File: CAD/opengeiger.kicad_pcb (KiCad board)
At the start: 2 copper layers, 91 x 43 mm, 58 parts, among them J1 Conn_01x02, J10 Conn_01x04, J2 Conn_01x02, J3 Conn_01x06, J4 Conn_01x02, J5 Conn_01x04, J6 Conn_01x04, J7 Conn_01x02, J8 USB_C_Receptacle_USB2.0, J9 Conn_01x04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

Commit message: feat: added interactive html bom
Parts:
- added R18: 10k, Resistor_SMD:R_0603_1608Metric_Pad0.98x0.95mm_HandSolder, F.Cu at (134.1, 102.4)
- Q3: value PMBT2222A,215 -> SI2301
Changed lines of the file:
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@@
     (tags "SOT-23")
     (property "INFO" "DIGIKEY")
-    (property "MPN" "PMBT2222A,215")
-    (property "Sheetfile" "opengeiger.kicad_sch")
-    (property "Sheetname" "")
-    (property "Supplier Part Number" "1727-2956-6-ND")
+    (property "MPN" "SI2302CDS-T1-GE3")
+    (property "Sheetfile" "opengeiger.kicad_sch")
+    (property "Sheetname" "")
+    (property "Supplier Part Number" "SI2302CDS-T1-GE3DKR-ND")
     (attr smd)
     (fp_text reference "Q3" (at 3.602 -1.362) (layer "F.SilkS")
       (effects (font (size 1 1) (thickness 0.15)))
     )
-    (fp_text value "PMBT2222A,215" (at 0 2.5) (layer "F.Fab")
+    (fp_text value "SI2301" (at 0 2.5) (layer "F.Fab")
       (effects (font (size 1 1) (thickness 0.15)))
     )
@@
       (net 16 "Net-(D5-Pad2)") (pintype "passive"))
     (model "${KIPRJMOD}/packages3D/R_0603_1608Metric.wrl"
+      (offset (xyz 0 0 0))
+      (scale (xyz 1 1 1))
+      (rotate (xyz 0 0 0))
+    )
+  )
+  (footprint "Resistor_SMD:R_0603_1608Metric_Pad0.98x0.95mm_HandSolder" (layer "F.Cu")
+    (at 134.112 102.362 90)
+    (descr "Resistor SMD 0603 (1608 Metric), square (rectangular) end terminal, IPC_7351 nominal with elongated pad for handsoldering. (Body size source: IPC-SM-782 page 72, https://www.pcb-3d.com/wordpress/wp-content/uploads/ipc-sm-782a_amendment_1_and_2.pdf), generated with kicad-footprint-generator")
+    (tags "resistor handsolder")
+    (property "INFO" "DIGIKEY")
+    (property "MPN" "RMCF0603JT10K0")
+    (property "Sheetfile" "opengeiger.kicad_sch")
+    (property "Sheetname" "")
+    (property "Supplier Part Number" "RMCF0603JT10K0DKR-ND")
+    (attr smd)
+    (fp_text reference "R18" (at 0 -1.43 90) (layer "F.SilkS")
+      (effects (font (size 1 1) (thickness 0.15)))
+    )
+    (fp_text value "10k" (at 0 1.43 90) (layer "F.Fab")
+      (effects (font (size 1 1) (thickness 0.15)))
+    )
+    (fp_text user "${REFERENCE}" (at 0 0 90) (layer "F.Fab")
+      (effects (font (size 0.4 0.4) (thickness 0.06)))
+    )
+    (fp_line (start -0.254724 -0.5225) (end 0.254724 -0.5225) (layer "F.SilkS") (width 0.12))
+    (fp_line (start -0.254724 0.5225) (end 0.254724 0.5225) (layer "F.SilkS") (width 0.12))
+    (fp_line (start 1.65 0.73) (end -1.65 0.73) (layer "F.CrtYd") (width 0.05))
+    (fp_line (start 1.65 -0.73) (end 1.65 0.73) (layer "F.CrtYd") (width 0.05))
+    (fp_line (start -1.65 0.73) (end -1.65 -0.73) (layer "F.CrtYd") (width 0.05))
+    (fp_line (start -1.65 -0.73) (end 1.65 -0.73) (layer "F.CrtYd") (width 0.05))
+    (fp_line (start 0.8 0.4125) (end -0.8 0.4125) (layer "F.Fab") (width 0.1))
+    (fp_line (start -0.8 0.4125) (end -0.8 -0.4125) (layer "F.Fab") (width 0.1))
+    (fp_line (start -0.8 -0.4125) (end 0.8 -0.4125) (layer "F.Fab") (width 0.1))
+    (fp_line (start 0.8 -0.4125) (end 0.8 0.4125) (layer "F.Fab") (width 0.1))
+    (pad "1" smd roundrect (at -0.9125 0 90) (size 0.975 0.95) (layers "F.Cu" "F.Paste" "F.Mask") (roundrect_rratio 0.25)
+      (net 2 "GNDREF") (pintype "passive"))
+    (pad "2" smd roundrect (at 0.9125 0 90) (size 0.975 0.95) (layers "F.Cu" "F.Paste" "F.Mask") (roundrect_rratio 0.25)
+      (net 30 "CLICKER") (pintype "passive"))
+    (model "${KICAD6_3DMODEL_DIR}/Resistor_SMD.3dshapes/R_0603_1608Metric.wrl"
       (offset (xyz 0 0 0))
       (scale (xyz 1 1 1))
@@
       (net 35 "unconnected-(U1-Pad12)") (pinfunction "IO27") (pintype "bidirectional+no_connect"))
     (pad "13" smd rect (at -8.5 6.985 90) (size 2 0.9) (layers "F.Cu" "F.Paste" "F.Mask")
-      (net 55 "unconnected-(U1-Pad13)") (pinfunction "IO14") (pintype "bidirectional"))
+      (net 55 "unconnected-(U1-Pad13)") (pinfunction "IO14") (pintype "bidirectional+no_connect"))
     (pad "14" smd rect (at -8.5 8.255 90) (size 2 0.9) (layers "F.Cu" "F.Paste" "F.Mask")
-      (net 56 "unconnected-(U1-Pad14)") (pinfunction "IO12") (pintype "bidirectional"))
+      (net 56 "unconnected-(U1-Pad14)") (pinfunction "IO12") (pintype "bidirectional+no_connect"))
     (pad "15" smd rect (at -5.715 9.255 180) (size 2 0.9) (layers "F.Cu" "F.Paste" "F.Mask")
       (net 2 "GNDREF") (pinfunction "GND") (pintype "passive"))
@@
       (net 41 "unconnected-(U1-Pad22)") (pinfunction "SDI/SD1") (pintype "bidirectional+no_connect"))
     (pad "23" smd rect (at 4.445 9.255 180) (size 2 0.9) (layers "F.Cu" "F.Paste" "F.Mask")
-      (net 57 "unconnected-(U1-Pad23)") (pinfunction "IO15") (pintype "bidirectional"))
+      (net 57 "unconnected-(U1-Pad23)") (pinfunction "IO15") (pintype "bidirectional+no_connect"))
     (pad "24" smd rect (at 5.715 9.255 180) (size 2 0.9) (layers "F.Cu" "F.Paste" "F.Mask")
       (net 58 "GPIO02") (pinfunction "IO2") (pintype "bidirectional"))

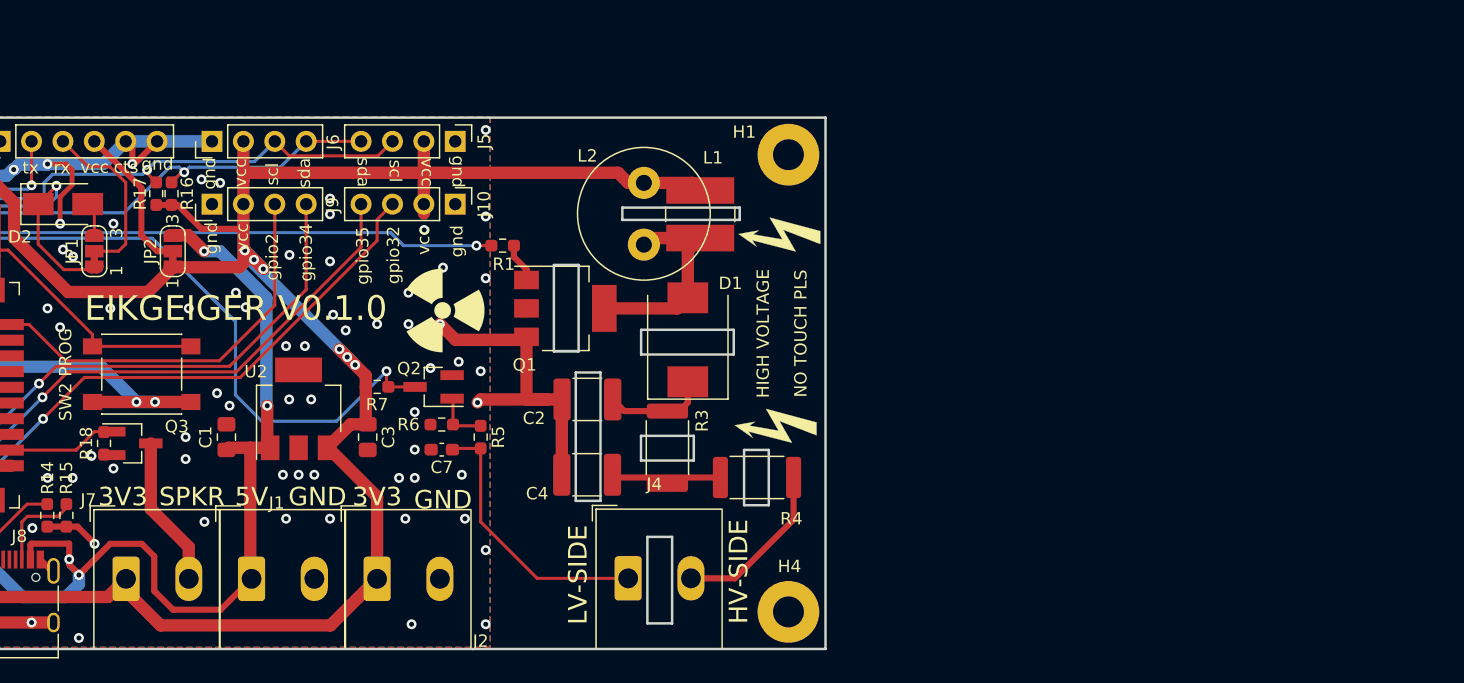
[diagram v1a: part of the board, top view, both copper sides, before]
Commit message: feat: 1206 version
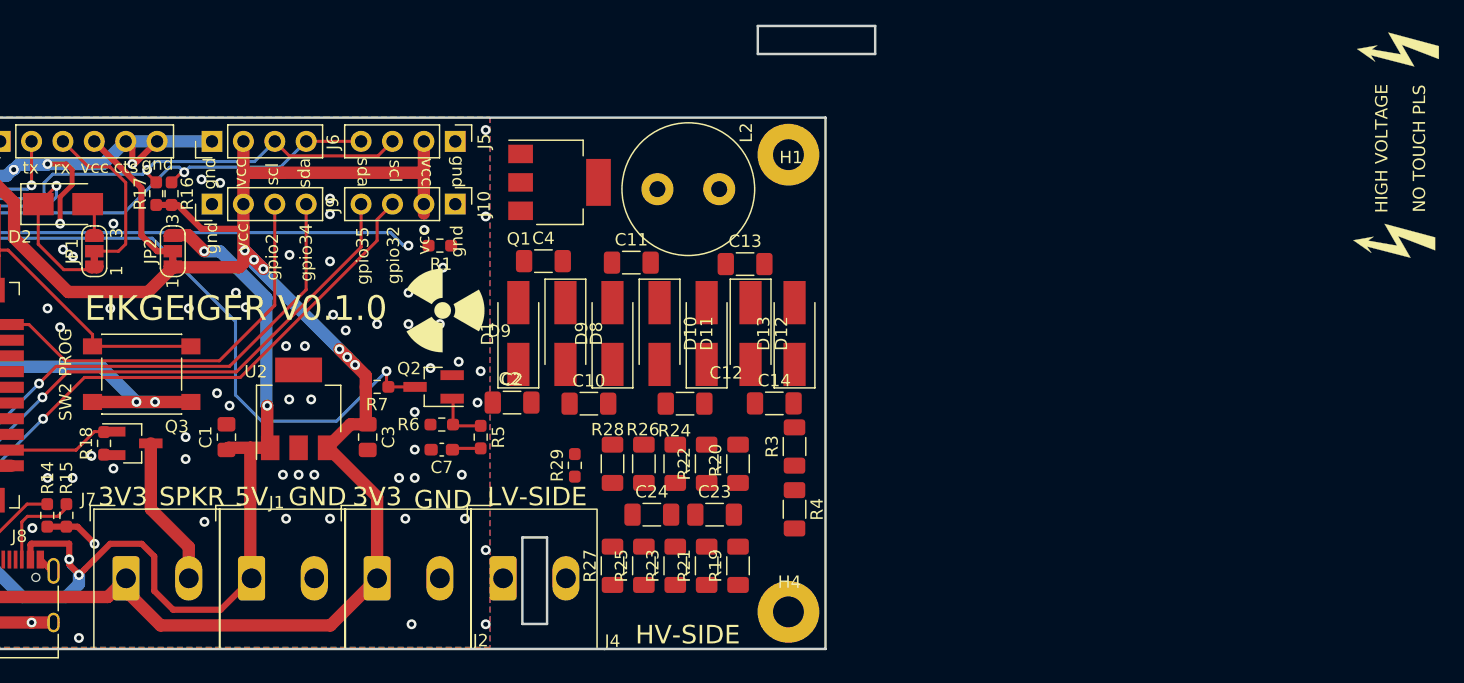
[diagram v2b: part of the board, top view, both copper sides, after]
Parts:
- removed L1: SDR0503-153JL, Inductor_SMD:L_TracoPower_TCK-047_5.2x5.8mm
- added C10: 330nF, Capacitor_SMD:C_1206_3216Metric_Pad1.33x1.80mm_HandSolder, F.Cu at (173.3, 99.1)
- added C11: 330nF, Capacitor_SMD:C_1206_3216Metric_Pad1.33x1.80mm_HandSolder, F.Cu at (176.8, 87.7)
- added C12: 330nF, Capacitor_SMD:C_1206_3216Metric_Pad1.33x1.80mm_HandSolder, F.Cu at (181.1, 99.1)
- added C13: 330nF, Capacitor_SMD:C_1206_3216Metric_Pad1.33x1.80mm_HandSolder, F.Cu at (186.0, 87.9)
- added C14: 330nF, Capacitor_SMD:C_1206_3216Metric_Pad1.33x1.80mm_HandSolder, F.Cu at (188.4, 99.1)
- added C23: 330nF, Capacitor_SMD:C_1206_3216Metric_Pad1.33x1.80mm_HandSolder, F.Cu at (183.5, 108.1)
- added C24: 330nF, Capacitor_SMD:C_1206_3216Metric_Pad1.33x1.80mm_HandSolder, F.Cu at (178.4, 108.1)
- added D10: RS1J, Diode_SMD:D_SMA_Handsoldering, F.Cu at (179.1, 93.5)
- added D11: RS1J, Diode_SMD:D_SMA_Handsoldering, F.Cu at (182.9, 93.5)
- added D12: RS1J, Diode_SMD:D_SMA_Handsoldering, F.Cu at (186.4, 93.5)
- added D13: RS1J, Diode_SMD:D_SMA_Handsoldering, F.Cu at (190.0, 93.5)
- added D8: RS1J, Diode_SMD:D_SMA_Handsoldering, F.Cu at (171.4, 93.5)
- added D9: RS1J, Diode_SMD:D_SMA_Handsoldering, F.Cu at (175.3, 93.5)
- added R19: 1M, Resistor_SMD:R_1206_3216Metric_Pad1.30x1.75mm_HandSolder, F.Cu at (185.4, 112.3)
- added R20: 1M, Resistor_SMD:R_1206_3216Metric_Pad1.30x1.75mm_HandSolder, F.Cu at (185.4, 104.0)
- added R21: 1M, Resistor_SMD:R_1206_3216Metric_Pad1.30x1.75mm_HandSolder, F.Cu at (182.9, 112.3)
- added R22: 1M, Resistor_SMD:R_1206_3216Metric_Pad1.30x1.75mm_HandSolder, F.Cu at (182.9, 104.0)
- added R23: 1M, Resistor_SMD:R_1206_3216Metric_Pad1.30x1.75mm_HandSolder, F.Cu at (180.3, 112.3)
- added R24: 1M, Resistor_SMD:R_1206_3216Metric_Pad1.30x1.75mm_HandSolder, F.Cu at (180.3, 104.0)
- added R25: 1M, Resistor_SMD:R_1206_3216Metric_Pad1.30x1.75mm_HandSolder, F.Cu at (177.8, 112.3)
- added R26: 1M, Resistor_SMD:R_1206_3216Metric_Pad1.30x1.75mm_HandSolder, F.Cu at (177.8, 104.0)
- added R27: 510k, Resistor_SMD:R_1206_3216Metric_Pad1.30x1.75mm_HandSolder, F.Cu at (175.3, 112.3)
- added R28: 1M, Resistor_SMD:R_1206_3216Metric_Pad1.30x1.75mm_HandSolder, F.Cu at (175.3, 104.0)
- added R29: 10k, Resistor_SMD:R_0603_1608Metric_Pad0.98x0.95mm_HandSolder, F.Cu at (172.2, 104.1)
- C2, C4: value 0.01uF/1kV -> 330nF; footprint Capacitor_SMD:C_1812_4532Metric -> Capacitor_SMD:C_1206_3216Metric_Pad1.33x1.80mm_HandSolder
- D1: value STTH212S -> RS1J; footprint Diode_SMD:D_SMC -> Diode_SMD:D_SMA_Handsoldering
- L2: value RLB1314-153KL -> 22mH
- R3: value 1M -> 510k; footprint Resistor_SMD:R_2512_6332Metric -> Resistor_SMD:R_1206_3216Metric_Pad1.30x1.75mm_HandSolder
- R4: value 4.7M -> 510k; footprint Resistor_SMD:R_2512_6332Metric -> Resistor_SMD:R_1206_3216Metric_Pad1.30x1.75mm_HandSolder
- moved C4 17.6 mm to (169.7, 87.6), turned to 0 degrees
- moved D1 13.7 mm to (167.6, 93.5)
- moved R3 10.3 mm to (190.0, 102.6), turned to 90 degrees
- moved Q1 10.2 mm to (171.0, 81.2)
- moved J4 10.1 mm to (166.4, 113.3)
- moved L2 6.12 mm to (183.9, 81.8), turned to 180 degrees
- moved C2 6.10 mm to (167.1, 99.1), turned to 0 degrees
- moved R1 5.08 mm to (161.3, 86.4)
- moved R4 3.98 mm to (190.0, 107.7), turned to -90 degrees
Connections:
- C2 pad 1: Net-(C2-Pad1) -> GNDREF
- C2 pad 2: GNDREF -> Net-(C10-Pad1)
- C4 pad 1: Net-(C4-Pad1) -> Net-(L2-Pad2)
- C4 pad 2: GNDREF -> Net-(C11-Pad1)
- D1 pad 1: Net-(C2-Pad1) -> Net-(C10-Pad1)
- D1 pad 2: Net-(D1-Pad2) -> Net-(L2-Pad2)
- L2 pad 2: Net-(D1-Pad2) -> Net-(L2-Pad2)
- Q1 pad 4: Net-(D1-Pad2) -> Net-(L2-Pad2)
- R3 pad 1: Net-(C2-Pad1) -> Net-(R3-Pad1)
- R3 pad 2: Net-(C4-Pad1) -> Net-(R3-Pad2)
- R4 pad 1: Net-(C4-Pad1) -> Net-(R3-Pad1)
- R4 pad 2: Net-(J4-Pad2) -> Net-(C23-Pad2)
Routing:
- net GNDREF: track 262.2 -> 234.8 mm, vias 99 -> 98
- net +3.3V: track 208.9 -> 185.9 mm
- net Net-(C7-Pad1): track 22.1 -> 2.33 mm
- net Net-(D1-Pad2): track 17.1 -> 0.00 mm
- net Net-(J4-Pad2): track 13.7 -> 0.00 mm
- net Net-(C4-Pad1): track 8.82 -> 0.00 mm
- net Net-(C2-Pad1): track 8.43 -> 0.00 mm
- net PWM: track 49.8 -> 43.1 mm
- net Net-(Q1-Pad1): track 3.20 -> 0.00 mm
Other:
- board size 91 x 43 mm -> 95 x 50.4 mm
- board text added: "330nF"
- board text added: "C2"
- board text added: "D9"

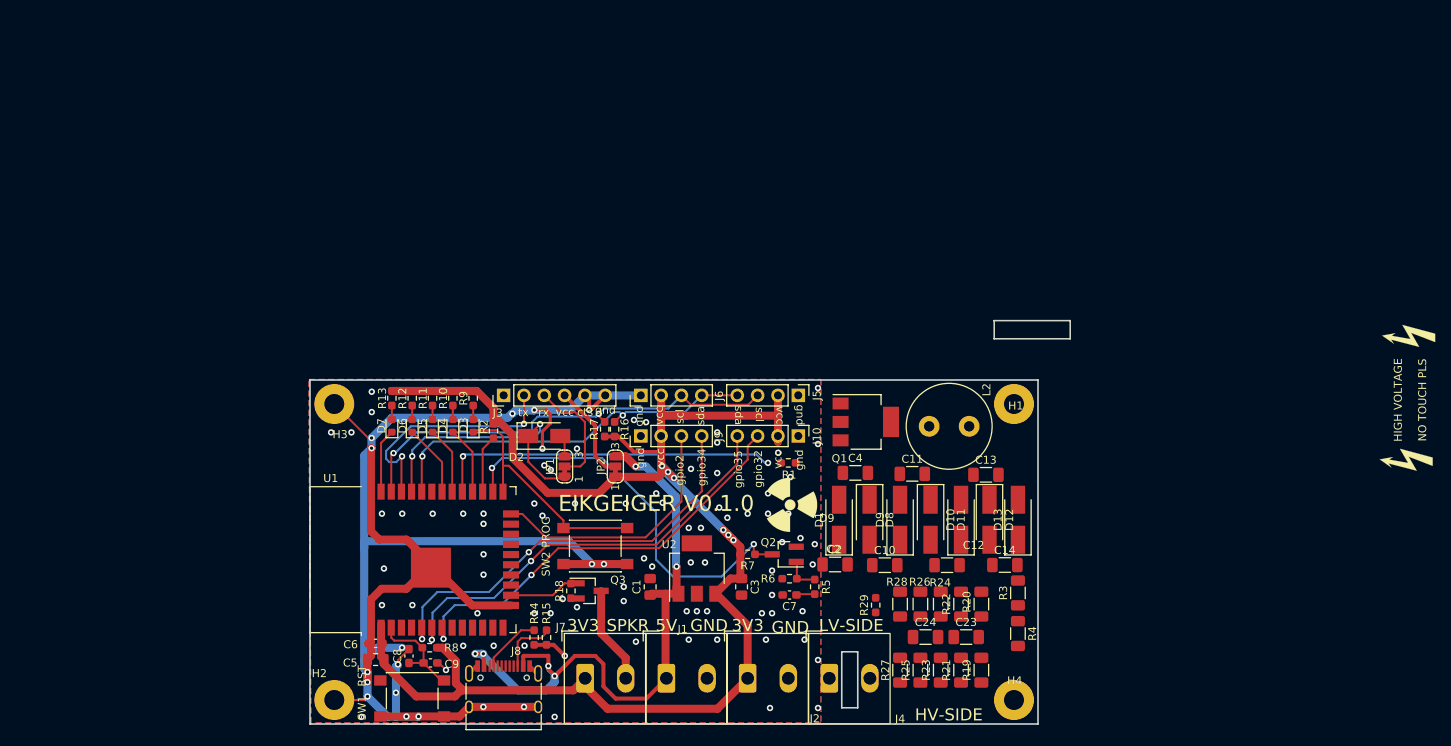
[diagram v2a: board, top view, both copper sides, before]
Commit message: Feat: Slimmify board
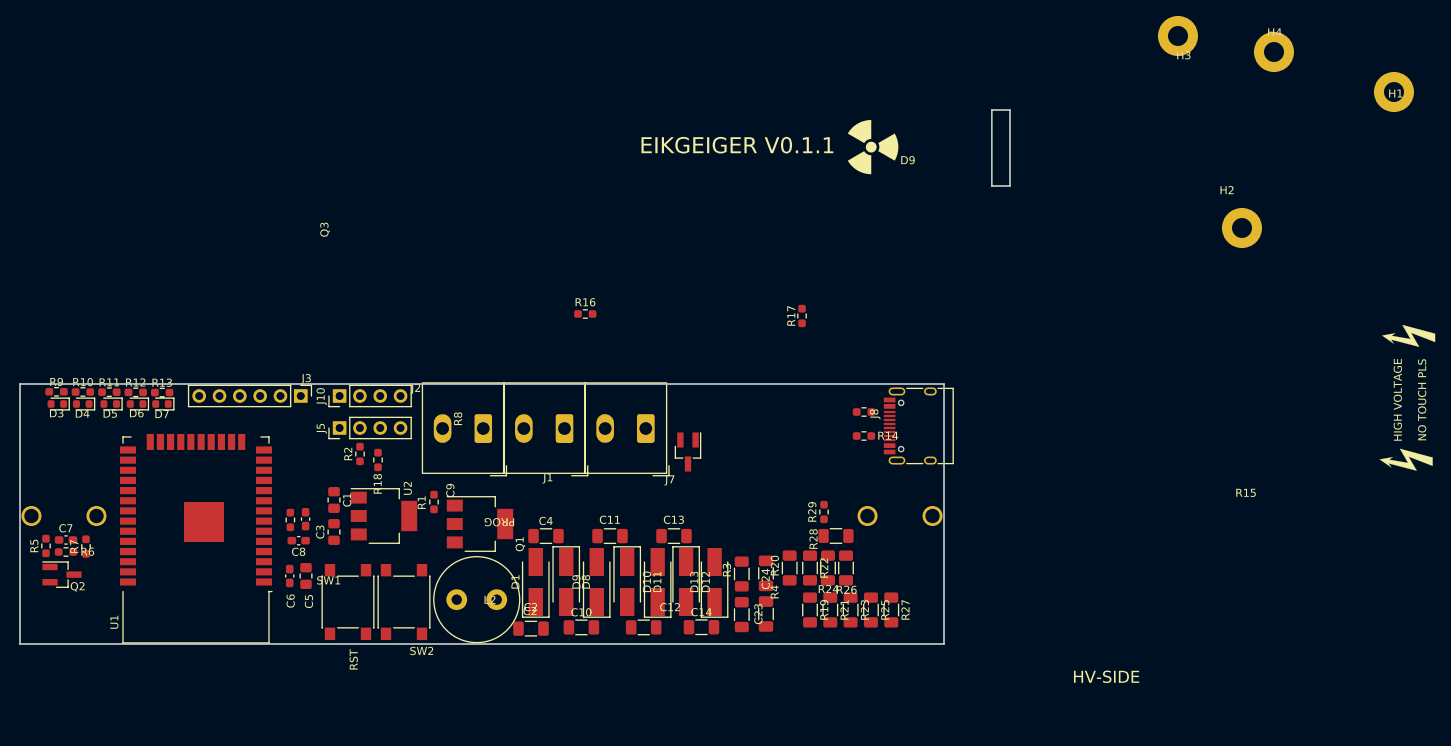
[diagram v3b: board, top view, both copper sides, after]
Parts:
- removed D2: VS-E7MH0112HM3/I, Diode_SMD:D_SMA
- removed J4: Conn_01x02, Fredriklib:TB010-508-02BE
- removed J6, J9: Conn_01x04, Connector_PinHeader_2.54mm:PinHeader_1x04_P2.54mm_Vertical
- removed JP1, JP2: SolderJumper_3_Bridged12, Jumper:SolderJumper-3_P1.3mm_Bridged12_RoundedPad1.0x1.5mm_NumberLabels
- added G*: SBM-20, eikgeiger:SBM-20, B.Cu at (123.0, 93.0)
- Q3: value SI2301 -> DMG2302UK-7
- R20, R22, R24, R26, R28: value 1M -> 10M
- R29: value 10k -> 100k
- U2: value AP7361C-33E -> TC1264-3.3VDBTR
- moved H2 127.9 mm to (218.0, 57.0)
- moved H3 115.1 mm to (210.0, 33.0)
- moved R5 96.2 mm to (68.5, 96.8), turned to 90 degrees
- moved C7 90.7 mm to (71.0, 96.0), turned to 0 degrees
- moved R6 90.5 mm to (71.0, 97.5), turned to 180 degrees
- moved Q2 90.3 mm to (70.5, 100.3), turned to 0 degrees
- moved H4 87.3 mm to (222.0, 35.0)
- moved R7 82.7 mm to (73.5, 96.8), turned to 90 degrees
- moved L2 67.6 mm to (119.8, 103.5), turned to 0 degrees
- moved J8 62.4 mm to (178.0, 81.8), turned to 90 degrees
- moved H1 61.5 mm to (237.0, 40.0)
- moved J10 57.6 mm to (105.2, 78.0), turned to 90 degrees
- moved J5 57.5 mm to (105.2, 82.0), turned to 90 degrees
- moved R9 52.1 mm to (69.8, 77.5), turned to 180 degrees
- moved D3 52.0 mm to (69.9, 79.0), turned to 180 degrees
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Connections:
- J3 pad 3: RX5V -> RXD
- J3 pad 4: VIN -> +3.3V
- R28 pad 2: Net-(R28-Pad2) -> RFB
- R29 pad 1: GNDREF -> RFB
- R29 pad 2: Net-(R28-Pad2) -> GNDREF
- U1 pad 10: unconnected-(U1-Pad10) -> RFB
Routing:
- net GNDREF: track 234.8 -> 0.00 mm, vias 98 -> 0
- net +3.3V: track 185.9 -> 0.00 mm, vias 6 -> 0
- net +5V: track 80.8 -> 0.00 mm, vias 6 -> 0
- net SCL: track 56.3 -> 0.00 mm, vias 2 -> 0
- net GPIO35: track 54.7 -> 0.00 mm, vias 2 -> 0
- net GPIO32: track 54.4 -> 0.00 mm, vias 2 -> 0
- net GPIO34: track 53.8 -> 0.00 mm, vias 2 -> 0
- net PULSE: track 51.0 -> 0.00 mm, vias 2 -> 0
- net SDA: track 49.0 -> 0.00 mm, vias 2 -> 0
- net PWM: track 43.1 -> 0.00 mm, vias 2 -> 0
- net RXD: track 33.9 -> 0.00 mm, vias 2 -> 0
- net GPIO02: track 32.6 -> 0.00 mm
- net PGM/GPIO0: track 30.4 -> 0.00 mm
- net TXD: track 30.1 -> 0.00 mm, vias 2 -> 0
- net RX5V: track 14.2 -> 0.00 mm
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- removed copper zone on B.Cu, net GNDREF
- removed copper zone on F.Cu, net GNDREF
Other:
- board size 95 x 50.4 mm -> 123.8 x 66.8 mm
- board text added: "EIKGEIGER V0.1.1"
- board text removed: "3V3"
- board text removed: "5V"
- board text removed: "EIKGEIGER V0.1.0"
- board text removed: "GND"
- board text removed: "LV-SIDE"
- board text removed: "SPKR"
- board text removed: "cts"
- board text removed: "gnd"
- board text removed: "gpio2"
- board text removed: "gpio32"
- board text removed: "gpio34"
- board text removed: "gpio35"
- board text removed: "rx"
- board text removed: "scl"
- board text removed: "sda"
- board text removed: "tx"
- board text removed: "vcc"
